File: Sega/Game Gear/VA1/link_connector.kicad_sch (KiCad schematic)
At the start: 10 parts

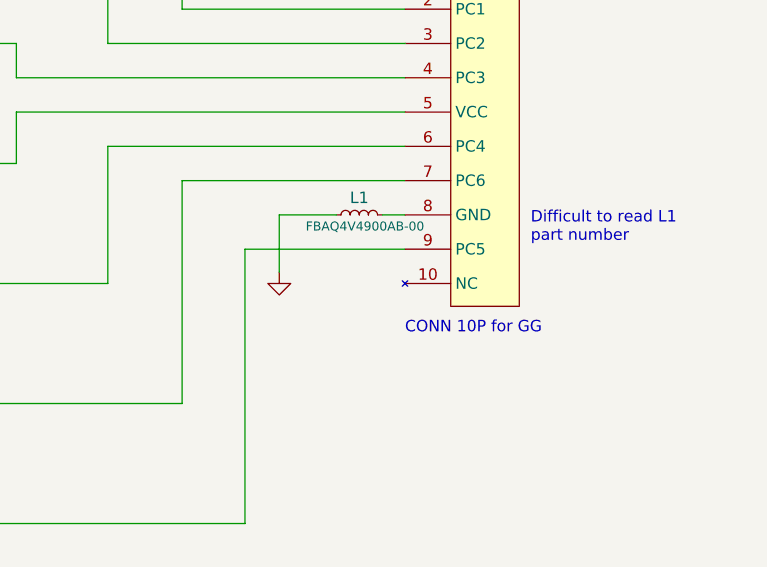
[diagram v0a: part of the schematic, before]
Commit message: Routed sound to LCD, created SND bus alias, created tv_sound alias, fixed issue where control and data intersected, changed serial conn to passive, finished minor signals on top of asic, power conn area, and started lcd routing.
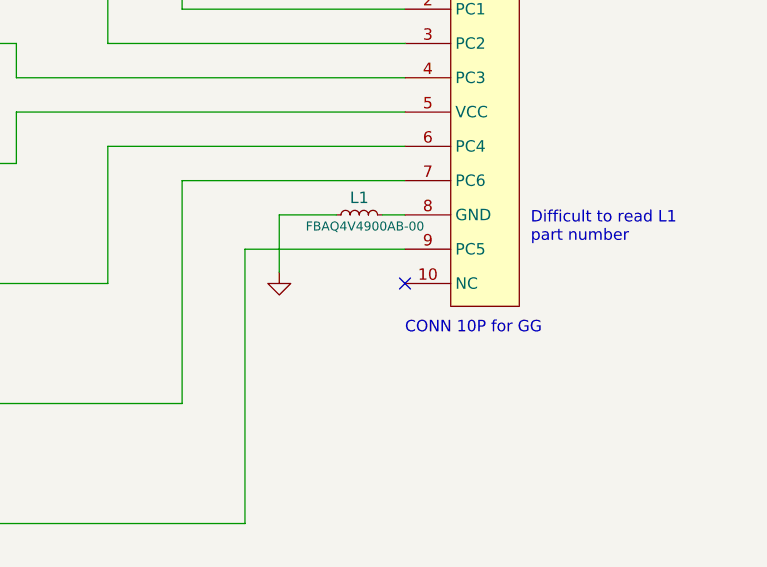
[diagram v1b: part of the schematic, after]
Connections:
- no-connect marks 0 -> 1
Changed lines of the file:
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@@
     (title "Link Connector")
   )
+  (no_connect (at 181.61 120.65))
   (wire (pts (xy 138.43 101.6) (xy 181.61 101.6))
     (stroke (width 0) (type default))

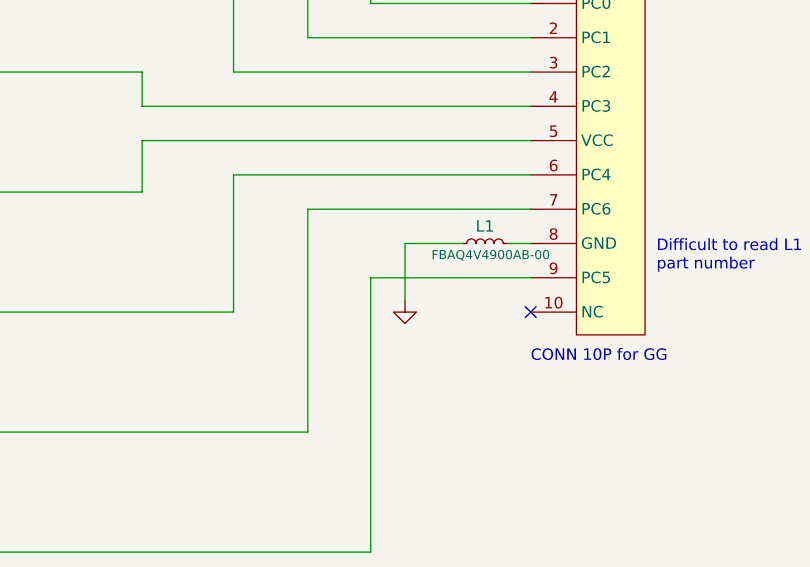
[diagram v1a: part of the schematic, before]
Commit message: GG VA1 passes ERC, needs review
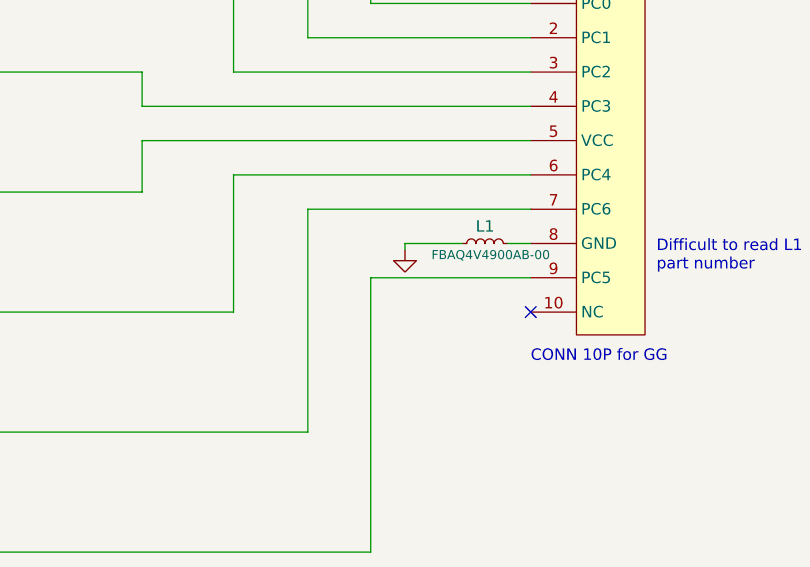
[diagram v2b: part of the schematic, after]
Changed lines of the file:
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@@
   (title_block
     (title "Link Connector")
+    (date "2023-02-07")
+    (rev "1")
+    (comment 1 "bald.ee/bitpreserve")
+    (comment 2 "Drawn by James Lewis (@baldengineer)")
   )
   (no_connect (at 181.61 120.65))
@@
     (stroke (width 0) (type default))
   )
-  (wire (pts (xy 167.64 113.03) (xy 167.64 119.38))
+  (wire (pts (xy 167.64 113.03) (xy 167.64 113.665))
     (stroke (width 0) (type default))
   )
@@
   )
   (text "Difficult to read L1\npart number" (at 195.58 116.205 0)
-    (effects (font (size 1.27 1.27)) (justify left bottom))
+    (effects (font (face "Verdana") (size 1.27 1.27)) (justify left bottom))
   )
   (hierarchical_label "PC4" (shape bidirectional) (at 102.235 120.65 180) (fields_autoplaced)
@@
     )
   )
-  (symbol (lib_id "power:GND") (at 167.64 119.38 0) (unit 1)
-    (in_bom yes) (on_board yes) (dnp no) (fields_autoplaced)
-    (property "Reference" "#PWR042" (at 167.64 125.73 0)
-      (effects (font (size 1.27 1.27)) hide)
-    )
-    (property "Value" "GND" (at 167.64 123.825 0)
-      (effects (font (size 1.27 1.27)) hide)
-    )
-    (property "Footprint" "" (at 167.64 119.38 0)
-      (effects (font (size 1.27 1.27)) hide)
-    )
-    (property "Datasheet" "" (at 167.64 119.38 0)
-      (effects (font (size 1.27 1.27)) hide)
-    )
+  (symbol (lib_id "power:GND") (at 167.64 113.665 0) (unit 1)
+    (in_bom yes) (on_board yes) (dnp no) (fields_autoplaced)
+    (property "Reference" "#PWR042" (at 167.64 120.015 0)
+      (effects (font (size 1.27 1.27)) hide)
+    )
+    (property "Value" "GND" (at 167.64 118.11 0)
+      (effects (font (size 1.27 1.27)) hide)
+    )
+    (property "Footprint" "" (at 167.64 113.665 0)
+      (effects (font (size 1.27 1.27)) hide)
+    )
+    (property "Datasheet" "" (at 167.64 113.665 0)
+      (effects (font (size 1.27 1.27)) hide)
+    )

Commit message: Game Gear v1 (VA1) PDFs
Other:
- company: (none) -> bald.ee/bitpreserve
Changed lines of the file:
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@@
   (title_block
     (title "Link Connector")
-    (date "2023-02-07")
+    (date "2023-02-14")
     (rev "1")
-    (comment 1 "bald.ee/bitpreserve")
-    (comment 2 "Drawn by James Lewis (@baldengineer)")
+    (company "bald.ee/bitpreserve")
+    (comment 1 "Drawn by James Lewis (@baldengineer)")
   )
   (no_connect (at 181.61 120.65))
